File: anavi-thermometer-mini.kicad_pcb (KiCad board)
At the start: 2 copper layers, 33 x 43.4 mm, 12 parts, among them SW1 SW_DIP_x01, U1 MOUDLE-SEEEDUINO-XIAO-ESP32C6, U2 DS18B20

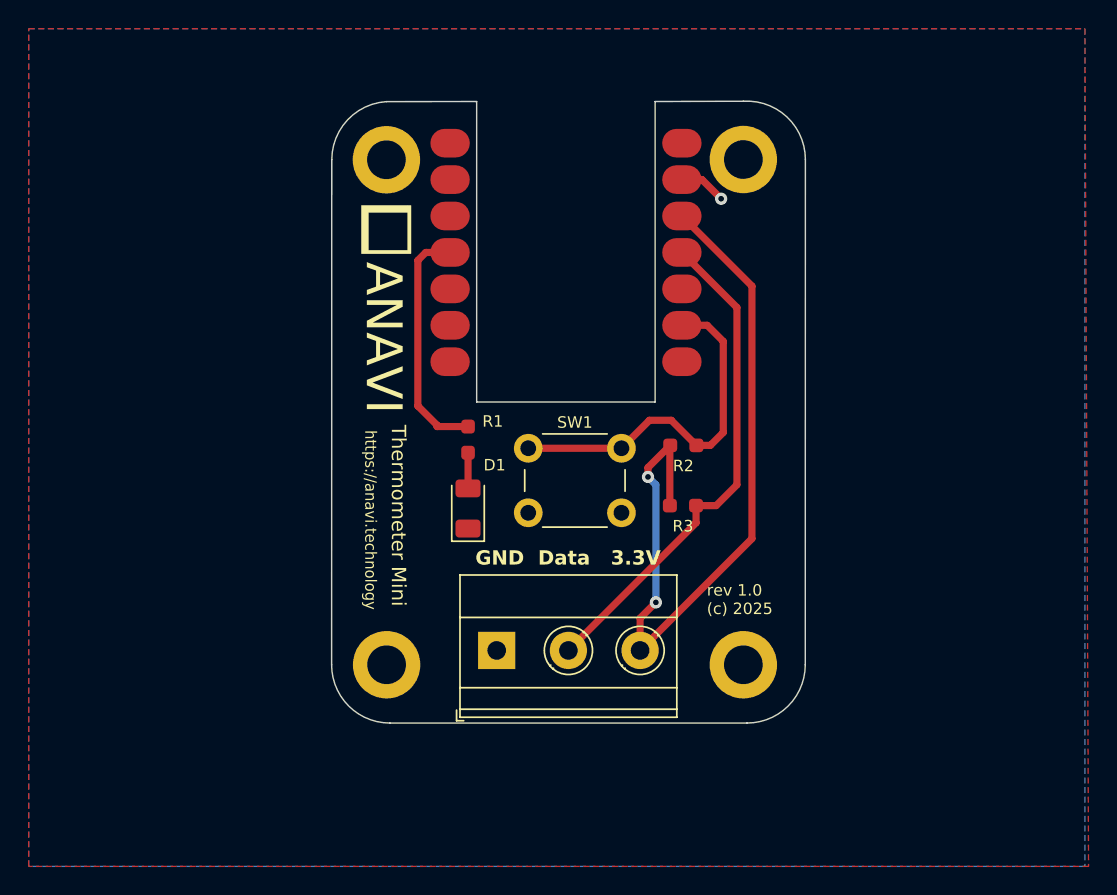
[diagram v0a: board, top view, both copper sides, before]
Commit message: Use WAGO 2059-303
Replace the three screw terminal block with the more compact
alternative WAGO 2059-303.

Signed-off-by: Leon Anavi <leon@anavi.org>
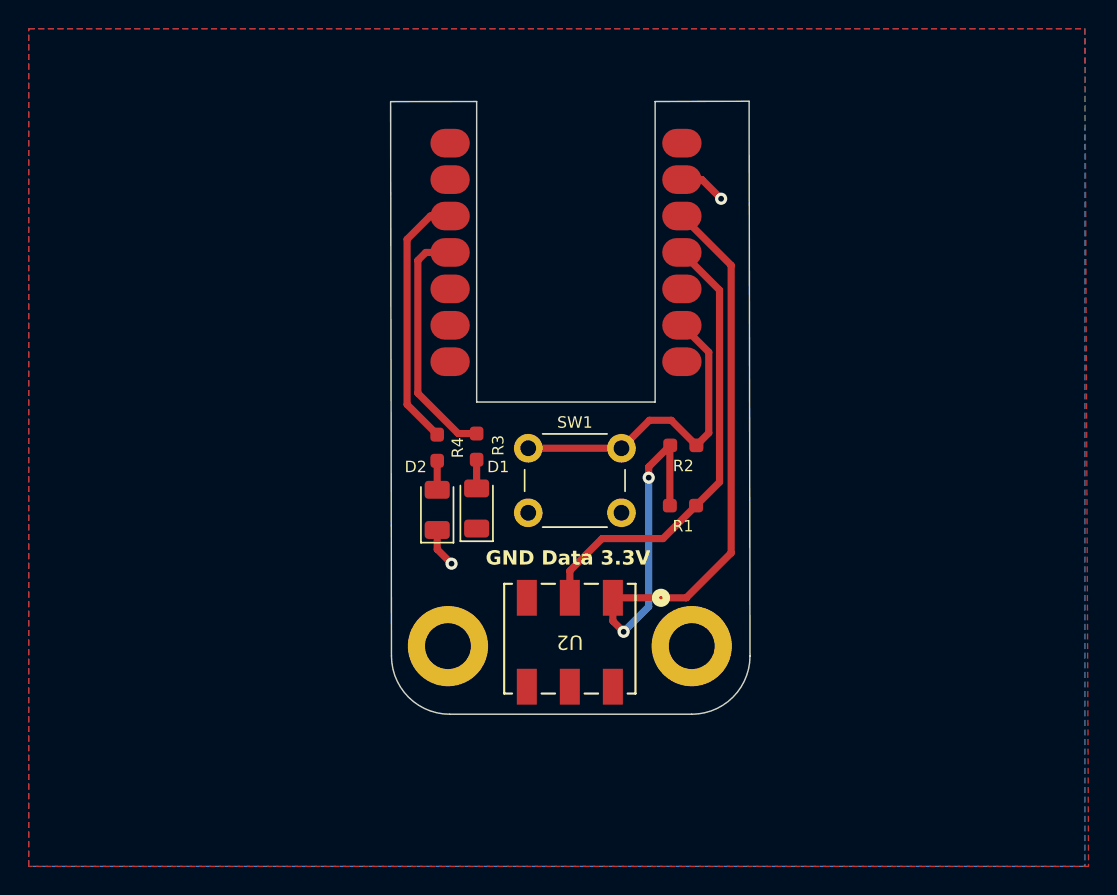
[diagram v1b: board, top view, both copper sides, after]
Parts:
- removed the REF** at (136.7, 72.3)
- removed the REF** at (136.7, 37.1)
- removed the REF** at (161.6, 37.1)
- removed the REF** at (161.6, 72.3)
- added D2: LED, LED_SMD:LED_1206_3216Metric, F.Cu at (140.2, 61.5)
- added R4: 68R, Resistor_SMD:R_0603_1608Metric_Pad0.98x0.95mm_HandSolder, F.Cu at (140.2, 57.2)
- added REF**: MountingHole_3.2mm_M3_DIN965_Pad, MountingHole:MountingHole_3.2mm_M3_DIN965_Pad, F.Cu at (141.0, 71.0)
- added REF**: MountingHole_3.2mm_M3_DIN965_Pad, MountingHole:MountingHole_3.2mm_M3_DIN965_Pad, F.Cu at (158.0, 71.0)
- G***: moved to B.Cu
- U2: footprint TerminalBlock_Phoenix:TerminalBlock_Phoenix_MKDS-1,5-3_1x03_P5.00mm_Horizontal -> footprints:CONN3_2059-303&slash_998-403_WAG
- moved G*** 6.78 mm to (139.9, 36.0)
- moved U2 5.17 mm to (149.5, 70.5), turned to 180 degrees
- moved R3 0.77 mm to (143.0, 57.1)
- moved D1 0.60 mm to (143.0, 61.4)
- renumbered R3 to R1, R1 to R3
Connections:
- U1 pad 3: unconnected-(U1-PA10_A2_D2-Pad3) -> Net-(U1-PA10_A2_D2)
- U2 pad 1: GND -> +3V3
- U2 pad 2: Net-(U1-PA6_A10_D10_MOSI) -> (no net)
- U2 pad 3: +3V3 -> Net-(U1-PA6_A10_D10_MOSI)
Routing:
- net Net-(U1-PA10_A2_D2): track 0.00 -> 18.2 mm
- net Net-(U1-PA6_A10_D10_MOSI): track 35.0 -> 32.0 mm
- net GND: track 3.29 -> 6.05 mm, vias 1 -> 2
- net Net-(U1-PA7_A8_D8_SCK): track 25.2 -> 22.8 mm
- net Net-(D2-A): track 0.00 -> 2.02 mm
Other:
- board size 33 x 43.4 mm -> 25.1 x 42.8 mm
- board text added: "rev 1.1 (c) 2025"
- board text removed: "rev 1.0 (c) 2025"
